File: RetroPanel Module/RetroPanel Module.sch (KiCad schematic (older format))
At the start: 56 parts, among them J1 Front Panel, J10 SW_EXTRA, J16 SPEAKER, J17 LED_HDD, J2 SW_POWER, J3 LED_POWER, J4 SW_RESET, J5 SW_TURBO, J6 LED_TURBO, J7 POWER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

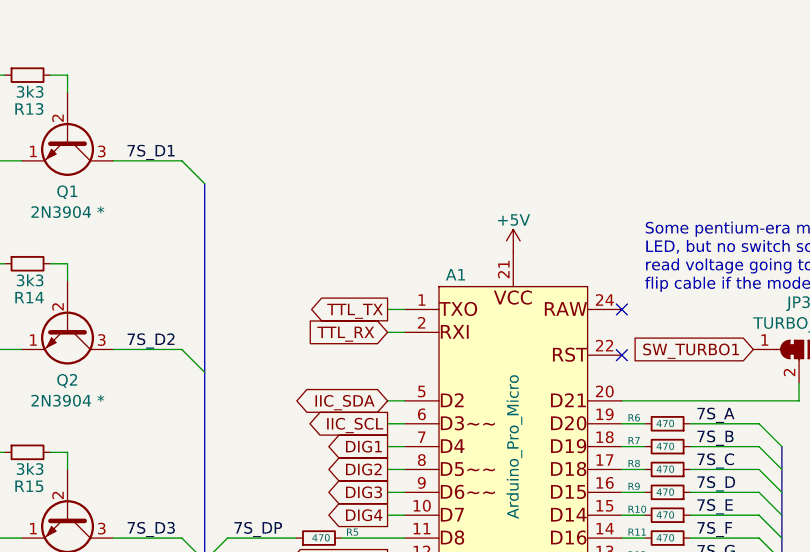
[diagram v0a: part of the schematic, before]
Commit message: Add external pullup for Serial1 RX
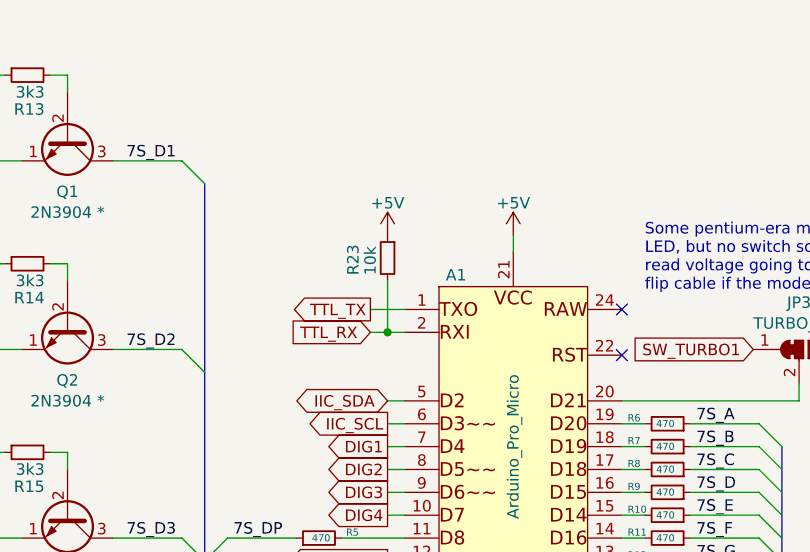
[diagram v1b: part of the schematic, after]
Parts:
- added R23: 10k, resistor:R_Axial_DIN0207_L6.3mm_D2.5mm_P10.16mm_Horizontal, symbol Device:R_Small
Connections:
- net +5V: now also R23.1
- net TTL_RX: now also R23.2
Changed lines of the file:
@@
 	1    0    0    -1
 $EndComp
-Wire Wire Line
-	6800 1850 6725 1850
-Text GLabel 6725 1850 0    50   Output ~ 0
+Text GLabel 6650 1850 0    50   Output ~ 0
 TTL_TX
-Text GLabel 6725 1950 0    50   Input ~ 0
+Text GLabel 6650 1950 0    50   Input ~ 0
 TTL_RX
 Wire Wire Line
@@
 L power:+5V #PWR0102
 U 1 1 6370FE93
-P 7275 1600
-F 0 "#PWR0102" H 7275 1450 50  0001 C CNN
-F 1 "+5V" H 7275 1740 50  0000 C CNN
-F 2 "" H 7275 1600 50  0000 C CNN
-F 3 "" H 7275 1600 50  0000 C CNN
-	1    7275 1600
+P 7275 1525
+F 0 "#PWR0102" H 7275 1375 50  0001 C CNN
+F 1 "+5V" H 7275 1665 50  0000 C CNN
+F 2 "" H 7275 1525 50  0000 C CNN
+F 3 "" H 7275 1525 50  0000 C CNN
+	1    7275 1525
 	1    0    0    -1
 $EndComp
@@
 Wire Wire Line
 	10325 1225 10450 1225
+$Comp
+L Device:R_Small R23
+U 1 1 6376B23E
+P 6725 1625
+F 0 "R23" V 6875 1550 50  0000 L CNN
+F 1 "10k" V 6800 1550 50  0000 L CNN
+F 2 "resistor:R_Axial_DIN0207_L6.3mm_D2.5mm_P10.16mm_Horizontal" H 6725 1625 50  0001 C CNN
+F 3 "~" H 6725 1625 50  0001 C CNN
+	1    6725 1625
+	-1   0    0    -1
+$EndComp
+Wire Wire Line
+	6650 1850 6800 1850
+Wire Wire Line
+	6725 1950 6650 1950
+Connection ~ 6725 1950
+$Comp
+L power:+5V #PWR0110
+U 1 1 637B1199
+P 6725 1525
+F 0 "#PWR0110" H 6725 1375 50  0001 C CNN
+F 1 "+5V" H 6725 1665 50  0000 C CNN
+F 2 "" H 6725 1525 50  0000 C CNN
+F 3 "" H 6725 1525 50  0000 C CNN
+	1    6725 1525
+	1    0    0    -1
+$EndComp
+Wire Wire Line
+	6725 1725 6725 1950
+Wire Wire Line
+	7275 1600 7275 1525
 Wire Bus Line
 	7950 4200 7950 4700

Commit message: Add mounting spot for DS3231 directly
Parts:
- added A2: IIC_RTC, RetroPanel:DS3231_ZS-042, symbol Connector_Generic:Conn_01x04
- D1: value 1N4001 -> 1N5819; symbol Diode:1N4001 -> Diode:1N5819
- LS1: value Speaker -> Passive Speaker; footprint Buzzer_Beeper:Buzzer_12x9.5RM7.6 -> small_buzzer:Buzzer_12x9.5RM7.6
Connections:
- net +5V: now also A2.3 (Pin_3)
- net GND: now also A2.4 (Pin_4)
- net IIC_SCL: now also A2.1 (Pin_1)
- net IIC_SDA: now also A2.2 (Pin_2)
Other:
- note added: "IIC_RTC pinout matches\nDS3231-module marked\n"ZS-042" with battery\nfacing up."
- moved on the sheet: J8, R1, R2
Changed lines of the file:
@@
 L Connector_Generic:Conn_01x04 J8
 U 1 1 637B3FDD
-P 875 3125
-F 0 "J8" H 793 3442 50  0000 C CNN
-F 1 "IIC" H 793 3351 50  0000 C CNN
-F 2 "Connector_PinHeader_2.54mm:PinHeader_1x04_P2.54mm_Vertical" H 875 3125 50  0001 C CNN
-F 3 "~" H 875 3125 50  0001 C CNN
-	1    875  3125
+P 800 3100
+F 0 "J8" H 800 3400 50  0000 C CNN
+F 1 "IIC" H 800 3325 50  0000 C CNN
+F 2 "Connector_PinHeader_2.54mm:PinHeader_1x04_P2.54mm_Vertical" H 800 3100 50  0001 C CNN
+F 3 "~" H 800 3100 50  0001 C CNN
+	1    800  3100
 	-1   0    0    -1
 $EndComp
@@
 L power:+5V #PWR01
 U 1 1 637B6165
-P 1150 2700
-F 0 "#PWR01" H 1150 2550 50  0001 C CNN
-F 1 "+5V" H 1150 2840 50  0000 C CNN
-F 2 "" H 1150 2700 50  0000 C CNN
-F 3 "" H 1150 2700 50  0000 C CNN
-	1    1150 2700
-	1    0    0    -1
-$EndComp
-Wire Wire Line
-	1150 2700 1150 2775
-Wire Wire Line
-	1150 3025 1075 3025
-Wire Wire Line
-	1075 3325 1150 3325
-Wire Wire Line
-	1150 3325 1150 3400
+P 1075 2675
+F 0 "#PWR01" H 1075 2525 50  0001 C CNN
+F 1 "+5V" H 1075 2815 50  0000 C CNN
+F 2 "" H 1075 2675 50  0000 C CNN
+F 3 "" H 1075 2675 50  0000 C CNN
+	1    1075 2675
+	1    0    0    -1
+$EndComp
+Wire Wire Line
+	1075 2675 1075 2750
+Wire Wire Line
+	1075 3000 1000 3000
 Text GLabel 6725 2350 0    50   Output ~ 0
 IIC_SCL
 Text GLabel 6725 2250 0    50   BiDi ~ 0
 IIC_SDA
-Text GLabel 1500 3225 2    50   Input ~ 0
+Text GLabel 1425 3200 2    50   Input ~ 0
 IIC_SCL
 $Comp
 L power:GND #PWR03
 U 1 1 637DE186
-P 1150 3400
-F 0 "#PWR03" H 1150 3150 50  0001 C CNN
-F 1 "GND" H 1155 3227 50  0000 C CNN
-F 2 "" H 1150 3400 50  0001 C CNN
-F 3 "" H 1150 3400 50  0001 C CNN
-	1    1150 3400
-	1    0    0    -1
-$EndComp
-Text GLabel 1500 3125 2    50   BiDi ~ 0
+P 1425 4150
+F 0 "#PWR03" H 1425 3900 50  0001 C CNN
+F 1 "GND" H 1430 3977 50  0000 C CNN
+F 2 "" H 1425 4150 50  0001 C CNN
+F 3 "" H 1425 4150 50  0001 C CNN
+	1    1425 4150
+	1    0    0    -1
+$EndComp
+Text GLabel 1425 3100 2    50   BiDi ~ 0
 IIC_SDA
 Wire Wire Line
@@
 L Device:R_Small R1
 U 1 1 63813303
-P 1350 2950
-F 0 "R1" H 1400 3000 50  0000 L CNN
-F 1 "4k7" H 1400 2925 50  0000 L CNN
-F 2 "resistor:R_Axial_DIN0207_L6.3mm_D2.5mm_P10.16mm_Horizontal" H 1350 2950 50  0001 C CNN
-F 3 "~" H 1350 2950 50  0001 C CNN
-	1    1350 2950
+P 1275 2925
+F 0 "R1" H 1325 2975 50  0000 L CNN
+F 1 "4k7" H 1325 2900 50  0000 L CNN
+F 2 "resistor:R_Axial_DIN0207_L6.3mm_D2.5mm_P10.16mm_Horizontal" H 1275 2925 50  0001 C CNN
+F 3 "~" H 1275 2925 50  0001 C CNN
+	1    1275 2925
 	-1   0    0    -1
 $EndComp
@@
 L Device:R_Small R2
 U 1 1 6381C91A
-P 1425 2950
-F 0 "R2" H 1475 2900 50  0000 L CNN
-F 1 "4k7" H 1475 2975 50  0000 L CNN
-F 2 "resistor:R_Axial_DIN0207_L6.3mm_D2.5mm_P10.16mm_Horizontal" H 1425 2950 50  0001 C CNN
-F 3 "~" H 1425 2950 50  0001 C CNN
-	1    1425 2950
+P 1350 2925
+F 0 "R2" H 1400 2875 50  0000 L CNN
+F 1 "4k7" H 1400 2950 50  0000 L CNN
+F 2 "resistor:R_Axial_DIN0207_L6.3mm_D2.5mm_P10.16mm_Horizontal" H 1350 2925 50  0001 C CNN
+F 3 "~" H 1350 2925 50  0001 C CNN
+	1    1350 2925
 	1    0    0    1
 $EndComp
 Wire Wire Line
-	1150 2775 1350 2775
-Wire Wire Line
-	1425 2775 1425 2850
-Wire Wire Line
-	1350 2850 1350 2775
-Wire Wire Line
-	1150 2775 1150 3025
-Connection ~ 1150 2775
-Connection ~ 1350 2775
-Wire Wire Line
-	1350 2775 1425 2775
-Wire Wire Line
-	1075 3125 1350 3125
-Wire Wire Line
-	1350 3050 1350 3125
-Connection ~ 1350 3125
-Wire Wire Line
-	1350 3125 1500 3125
-Wire Wire Line
-	1425 3050 1425 3225
-Wire Wire Line
-	1075 3225 1425 3225
-Wire Wire Line
-	1425 3225 1500 3225
-Connection ~ 1425 3225
+	1075 2750 1275 2750
+Wire Wire Line
+	1350 2750 1350 2825
+Wire Wire Line
+	1275 2825 1275 2750
+Wire Wire Line
+	1075 2750 1075 3000
+Connection ~ 1075 2750
+Connection ~ 1275 2750
+Wire Wire Line
+	1275 2750 1350 2750
+Wire Wire Line
+	1000 3100 1275 3100
+Wire Wire Line
+	1275 3025 1275 3100
+Connection ~ 1275 3100
+Wire Wire Line
+	1275 3100 1425 3100
+Wire Wire Line
+	1350 3025 1350 3200
+Wire Wire Line
+	1000 3200 1350 3200
+Wire Wire Line
+	1350 3200 1425 3200
+Connection ~ 1350 3200
 Text GLabel 6725 2950 0    50   Output ~ 0
 ARD_PWR
@@
 P 2225 6100
 F 0 "LS1" H 2188 6417 50  0000 C CNN
-F 1 "Speaker" H 2188 6326 50  0000 C CNN
-F 2 "Buzzer_Beeper:Buzzer_12x9.5RM7.6" H 2225 5900 50  0001 C CNN
+F 1 "Passive Speaker" H 2188 6326 50  0000 C CNN
+F 2 "small_buzzer:Buzzer_12x9.5RM7.6" H 2225 5900 50  0001 C CNN
 F 3 "~" H 2215 6050 50  0001 C CNN
 	1    2225 6100
@@
 	10250 3850 10325 3850
 $Comp
-L Diode:1N4001 D1
+L Diode:1N5819 D1
 U 1 1 635B47F3
 P 725 1500
 F 0 "D1" V 771 1420 50  0000 R CNN
-F 1 "1N4001" V 680 1420 50  0000 R CNN
+F 1 "1N5819" V 680 1420 50  0000 R CNN
 F 2 "Diode_THT:D_DO-41_SOD81_P10.16mm_Horizontal" H 725 1325 50  0001 C CNN
 F 3 "http://www.vishay.com/docs/88503/1n4001.pdf" H 725 1500 50  0001 C CNN
@@
 Wire Wire Line
 	7275 1600 7275 1525
+$Comp
+L Connector_Generic:Conn_01x04 A2
+U 1 1 638C2E4A
+P 800 3875
+F 0 "A2" H 800 4175 50  0000 C CNN
+F 1 "IIC_RTC" H 800 4100 50  0000 C CNN
+F 2 "RetroPanel:DS3231_ZS-042" H 800 3875 50  0001 C CNN
+F 3 "~" H 800 3875 50  0001 C CNN
+	1    800  3875
+	-1   0    0    -1
+$EndComp
+Wire Wire Line
+	1000 3300 1425 3300
+Wire Wire Line
+	1000 4075 1425 4075
+Connection ~ 1425 4075
+Wire Wire Line
+	1425 4075 1425 4150
+Wire Wire Line
+	1075 3975 1000 3975
+Wire Wire Line
+	1000 3875 1275 3875
+Wire Wire Line
+	1350 3775 1000 3775
+Text Notes 675  4700 0    50   ~ 0
+IIC_RTC pinout matches\nDS3231-module marked\n"ZS-042" with battery\nfacing up.
+Wire Wire Line
+	1075 3000 1075 3975
+Connection ~ 1075 3000
+Wire Wire Line
+	1275 3100 1275 3875
+Wire Wire Line
+	1350 3200 1350 3775
+Wire Wire Line
+	1425 3300 1425 4075
 Wire Bus Line
 	7950 4200 7950 4700

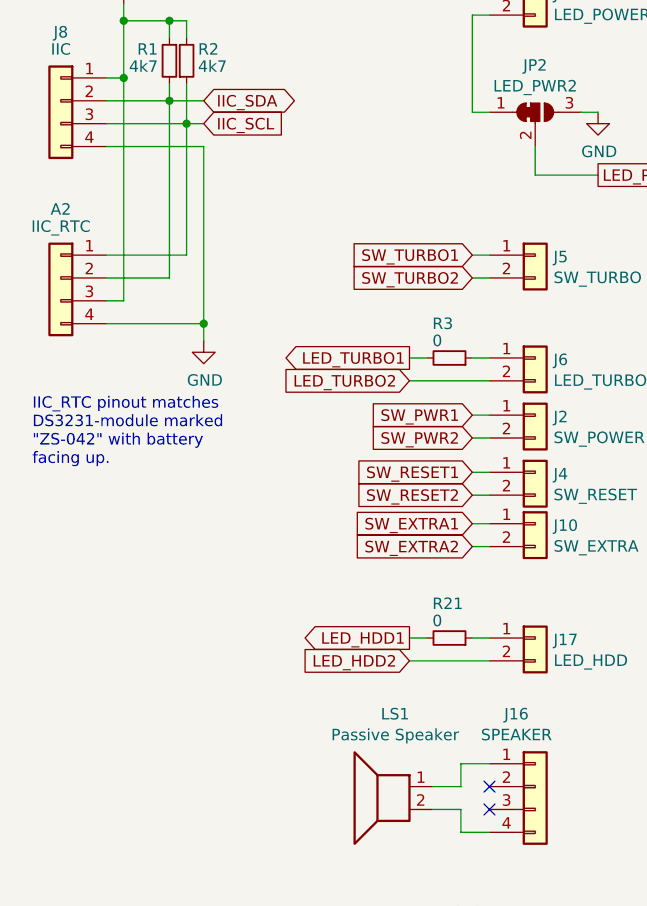
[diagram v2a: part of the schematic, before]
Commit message: Adjust cutout to move unit forward
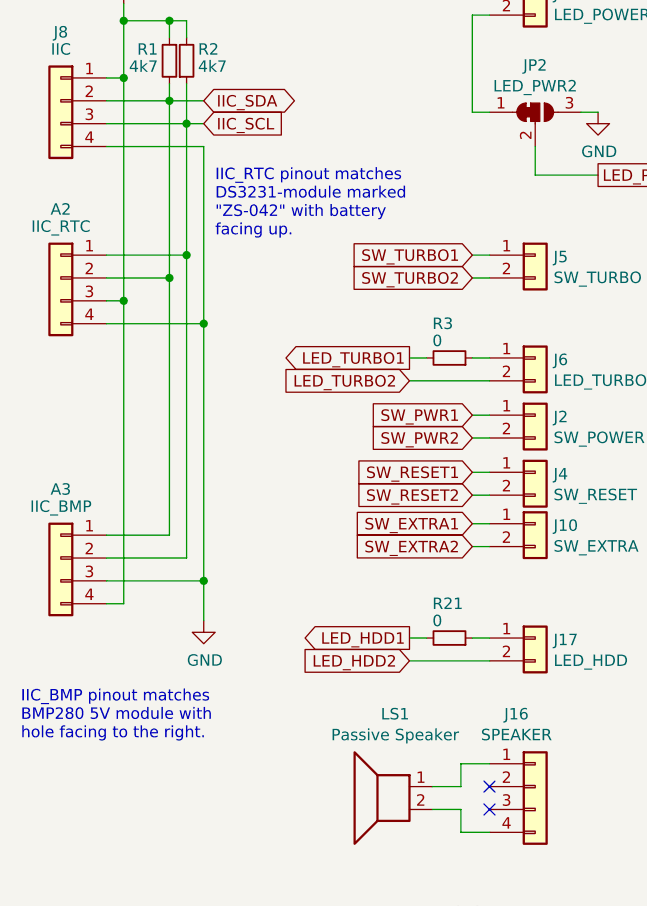
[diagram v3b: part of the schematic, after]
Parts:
- added A3: IIC_BMP, RetroPanel:BMP280-5V, symbol Connector_Generic:Conn_01x04
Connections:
- net +5V: now also A3.4 (Pin_4)
- net GND: now also A3.3 (Pin_3)
- net IIC_SCL: now also A3.2 (Pin_2)
- net IIC_SDA: now also A3.1 (Pin_1)
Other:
- note added: "IIC_BMP pinout matches\nBMP280 5V module with\nhole facing to the right."
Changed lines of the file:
@@
 L power:GND #PWR03
 U 1 1 637DE186
-P 1425 4150
-F 0 "#PWR03" H 1425 3900 50  0001 C CNN
-F 1 "GND" H 1430 3977 50  0000 C CNN
-F 2 "" H 1425 4150 50  0001 C CNN
-F 3 "" H 1425 4150 50  0001 C CNN
-	1    1425 4150
+P 1425 5375
+F 0 "#PWR03" H 1425 5125 50  0001 C CNN
+F 1 "GND" H 1430 5202 50  0000 C CNN
+F 2 "" H 1425 5375 50  0001 C CNN
+F 3 "" H 1425 5375 50  0001 C CNN
+	1    1425 5375
 	1    0    0    -1
 $EndComp
@@
 Connection ~ 1425 4075
 Wire Wire Line
-	1425 4075 1425 4150
-Wire Wire Line
 	1075 3975 1000 3975
 Wire Wire Line
@@
 Wire Wire Line
 	1350 3775 1000 3775
-Text Notes 675  4700 0    50   ~ 0
+Text Notes 1475 3700 0    50   ~ 0
 IIC_RTC pinout matches\nDS3231-module marked\n"ZS-042" with battery\nfacing up.
 Wire Wire Line
@@
 Wire Wire Line
 	1425 3300 1425 4075
+$Comp
+L Connector_Generic:Conn_01x04 A3
+U 1 1 63941B37
+P 800 5100
+F 0 "A3" H 800 5400 50  0000 C CNN
+F 1 "IIC_BMP" H 800 5325 50  0000 C CNN
+F 2 "RetroPanel:BMP280-5V" H 800 5100 50  0001 C CNN
+F 3 "~" H 800 5100 50  0001 C CNN
+	1    800  5100
+	-1   0    0    -1
+$EndComp
+Wire Wire Line
+	1425 4075 1425 5200
+Wire Wire Line
+	1000 5200 1425 5200
+Connection ~ 1425 5200
+Wire Wire Line
+	1425 5200 1425 5375
+Wire Wire Line
+	1075 3975 1075 5300
+Wire Wire Line
+	1075 5300 1000 5300
+Connection ~ 1075 3975
+Wire Wire Line
+	1000 5100 1350 5100
+Wire Wire Line
+	1350 5100 1350 3775
+Connection ~ 1350 3775
+Wire Wire Line
+	1275 3875 1275 5000
+Wire Wire Line
+	1275 5000 1000 5000
 Wire Bus Line
 	7950 4200 7950 4700
@@
 Wire Bus Line
 	9375 2650 9375 3850
+Connection ~ 1275 3875
+Text Notes 625  5900 0    50   ~ 0
+IIC_BMP pinout matches\nBMP280 5V module with\nhole facing to the right.
 $EndSCHEMATC
